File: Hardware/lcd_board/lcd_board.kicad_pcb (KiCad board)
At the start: 2 copper layers, 80.8 x 60.1 mm, 18 parts, among them J1 Conn_01x40, J2 Conn_01x16, U1 74HC04, U2 74HC173, U3 74HC173, U4 74HC174

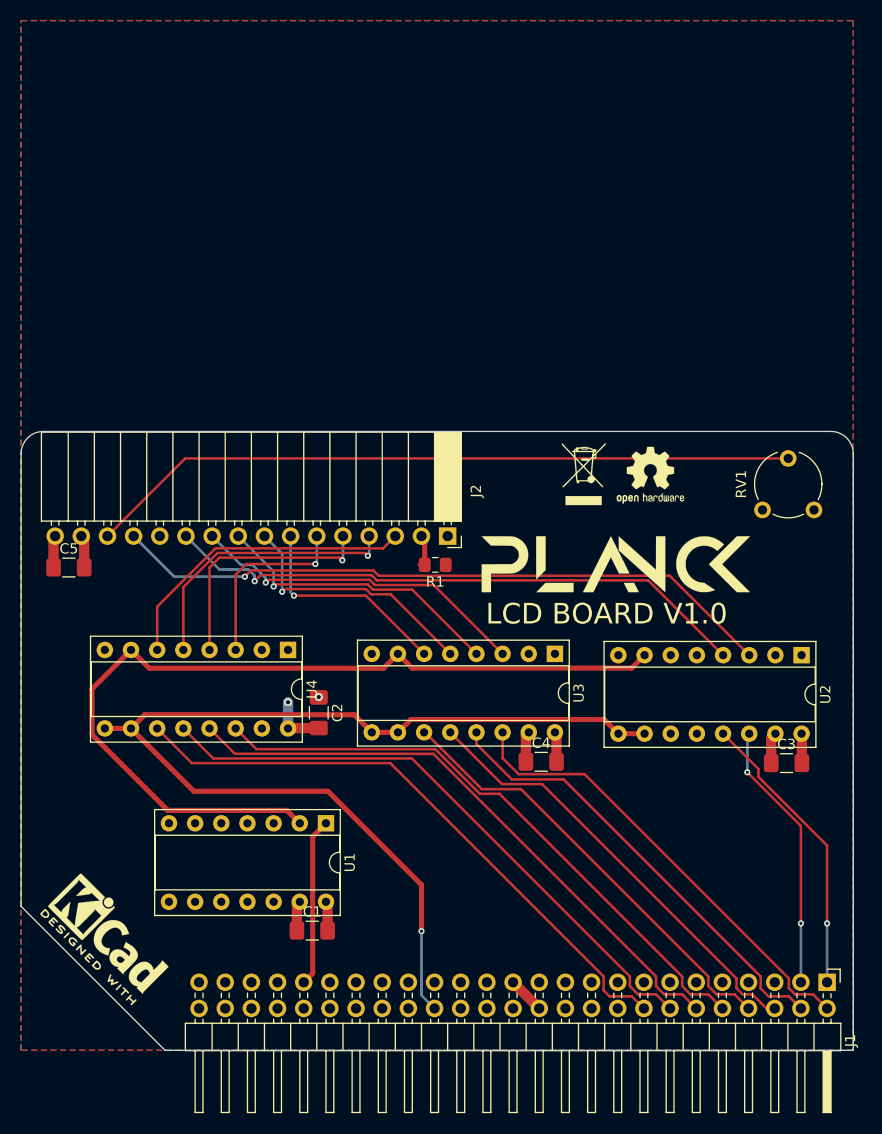
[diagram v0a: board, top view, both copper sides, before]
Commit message: LCD board with through hole components
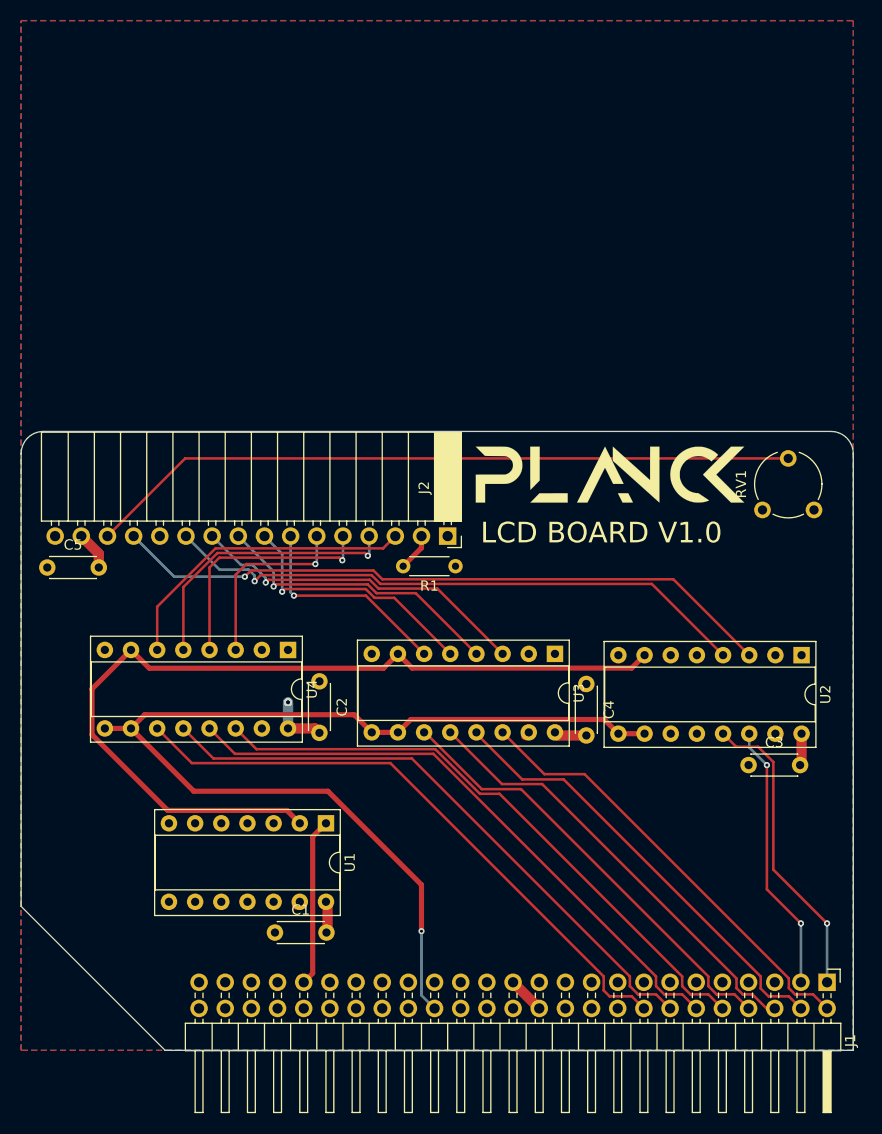
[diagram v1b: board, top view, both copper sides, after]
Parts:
- removed the G*** at (64.5, -47.1)
- removed the G*** at (57.7, -47.2)
- removed REF**: OSHW-Logo2_7.3x6mm_SilkScreen, Symbol:OSHW-Logo2_7.3x6mm_SilkScreen
- removed REF**: WEEE-Logo_4.2x6mm_SilkScreen, Symbol:WEEE-Logo_4.2x6mm_SilkScreen
- removed REF**: KiCad-Logo2_5mm_SilkScreen, Symbol:KiCad-Logo2_5mm_SilkScreen
- added G***: LOGO, Logo:logo, B.Cu at (64.5, -47.5)
- added G***: LOGO, Logo:logo, F.Cu at (57.1, -55.9)
- C1, C2, C3, C4, C5: value C_Small -> 4.7u; footprint Capacitor_SMD:C_1206_3216Metric_Pad1.42x1.75mm_HandSolder -> Capacitor_THT:C_Disc_D4.3mm_W1.9mm_P5.00mm
- R1: footprint Resistor_SMD:R_0805_2012Metric_Pad1.15x1.40mm_HandSolder -> Resistor_THT:R_Axial_DIN0204_L3.6mm_D1.6mm_P5.08mm_Horizontal
- U4: value 74HC174 -> 74HC173
- moved C4 8.73 mm to (54.9, -35.6), turned to 270 degrees
- moved C3 3.69 mm to (70.6, -27.7)
- moved C1 3.62 mm to (24.6, -11.4)
- moved C2 3.05 mm to (29.0, -35.8)
- moved C5 2.10 mm to (2.54, -46.9)
- moved R1 1.97 mm to (42.2, -47.0)
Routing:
- net GND: track 12.0 -> 1.01 mm, vias 1 -> 0
- net D0: track 44.6 -> 43.1 mm
- net +5V: track 20.9 -> 22.2 mm
- net A0: track 28.3 -> 29.6 mm
- net D1: track 43.9 -> 43.4 mm

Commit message: update lcd board
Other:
- rule pad_to_mask_clearance: 0.05 -> 0
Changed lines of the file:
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@@
     (pad_size 3.8 3.8)
     (pad_drill 2.2)
-    (pad_to_mask_clearance 0.05)
+    (pad_to_mask_clearance 0)
     (aux_axis_origin 0 0)
     (visible_elements FFFFFF7F)

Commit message: final update for through hole conversion
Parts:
- C1, C2, C3, C4, C5: value 4.7u -> 10n

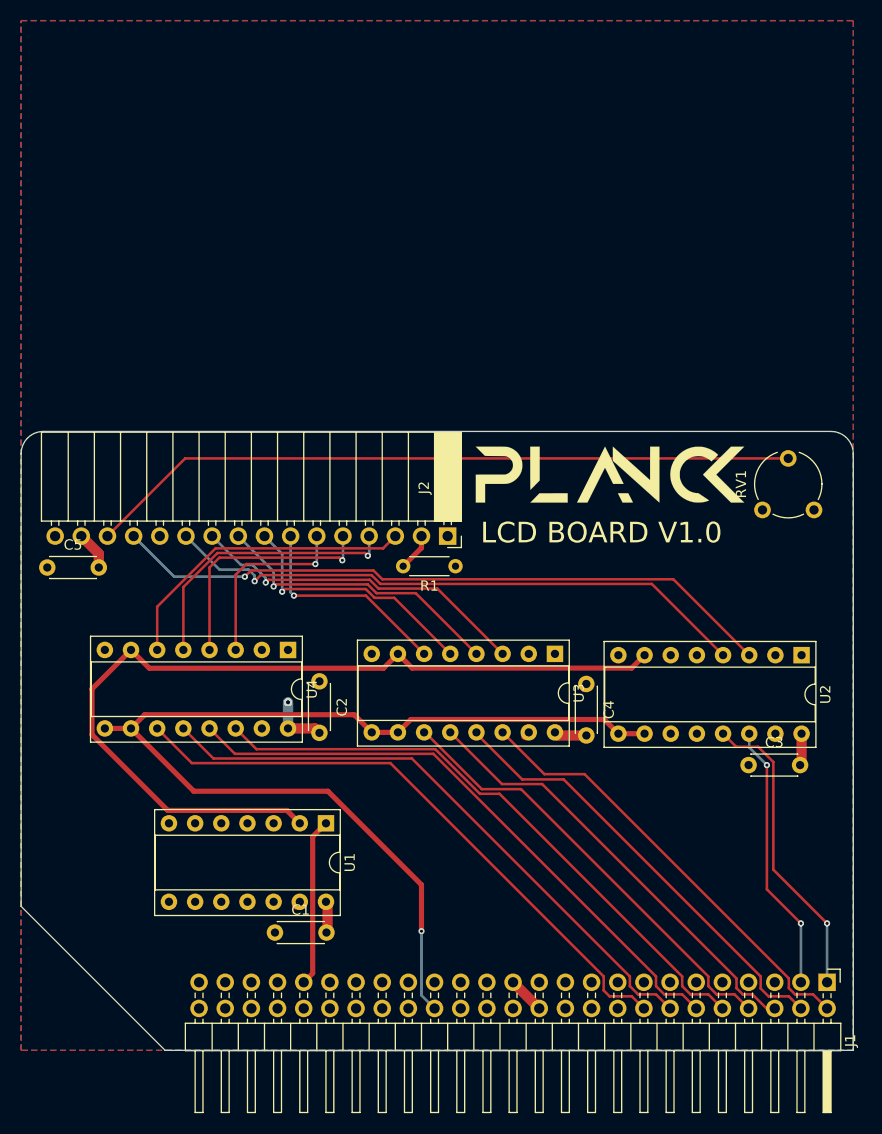
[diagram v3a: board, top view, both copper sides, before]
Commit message: update lcd board with bigger resistors
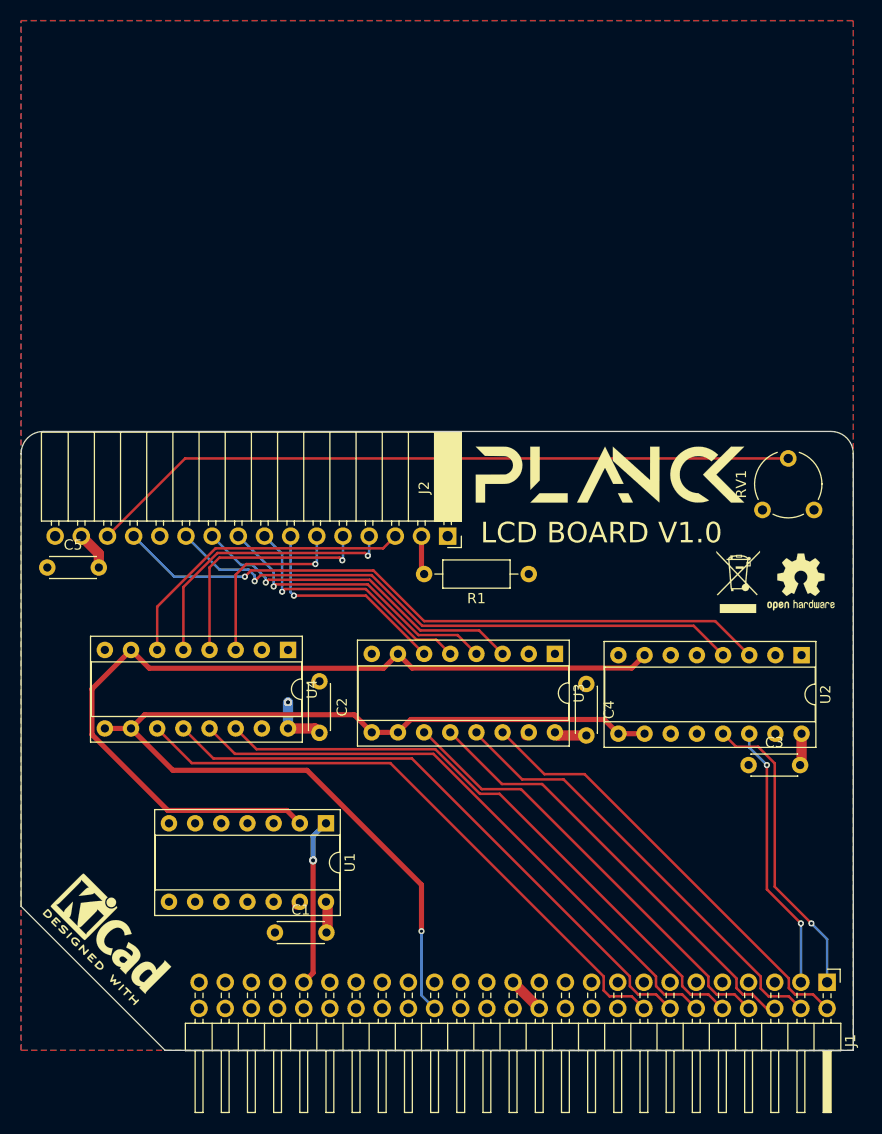
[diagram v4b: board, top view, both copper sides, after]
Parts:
- added REF**: KiCad-Logo2_5mm_SilkScreen, Symbol:KiCad-Logo2_5mm_SilkScreen, F.Cu at (8.64, -10.9)
- added REF**: WEEE-Logo_4.2x6mm_SilkScreen, Symbol:WEEE-Logo_4.2x6mm_SilkScreen, F.Cu at (69.6, -45.5)
- added REF**: OSHW-Logo2_7.3x6mm_SilkScreen, Symbol:OSHW-Logo2_7.3x6mm_SilkScreen, F.Cu at (75.7, -45.5)
- R1: footprint Resistor_THT:R_Axial_DIN0204_L3.6mm_D1.6mm_P5.08mm_Horizontal -> Resistor_THT:R_Axial_DIN0207_L6.3mm_D2.5mm_P10.16mm_Horizontal
- moved G*** 11.2 mm to (57.1, -55.9)
- moved R1 7.15 mm to (49.3, -46.2)
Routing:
- net CLK: vias 0 -> 1
